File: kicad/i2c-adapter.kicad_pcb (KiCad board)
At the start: 2 copper layers, 98.4 x 65 mm, 49 parts, among them J1 Conn_02x13_Top_Bottom, J10 AUX IN, J11 +5V, J2 I2C-1, J3 I2C-2, J4 I2C-3, J5 I2C-4, J6 SPI-1, J7 SPI-2, J8 SPI-3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

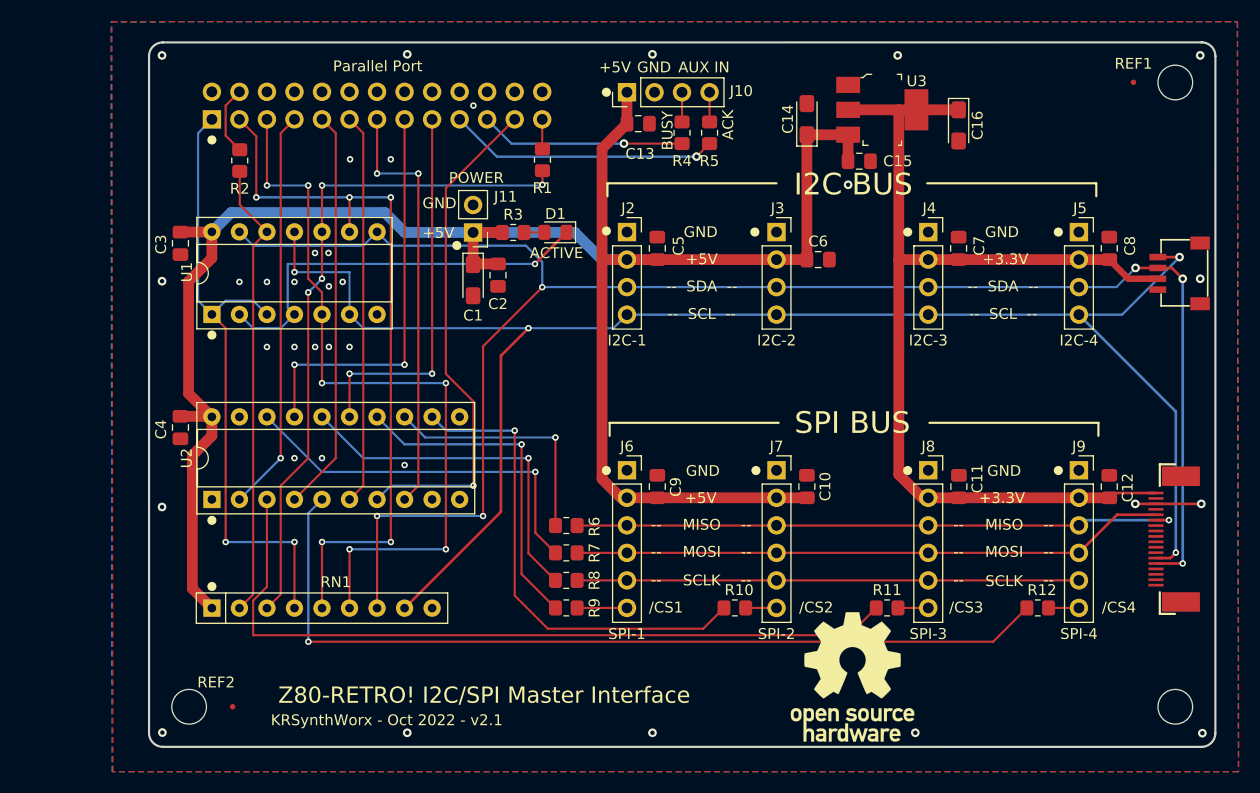
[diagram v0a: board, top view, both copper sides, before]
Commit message: Finish up cleanup of both Schematic and PCB; Give Adafruit connectors labels.
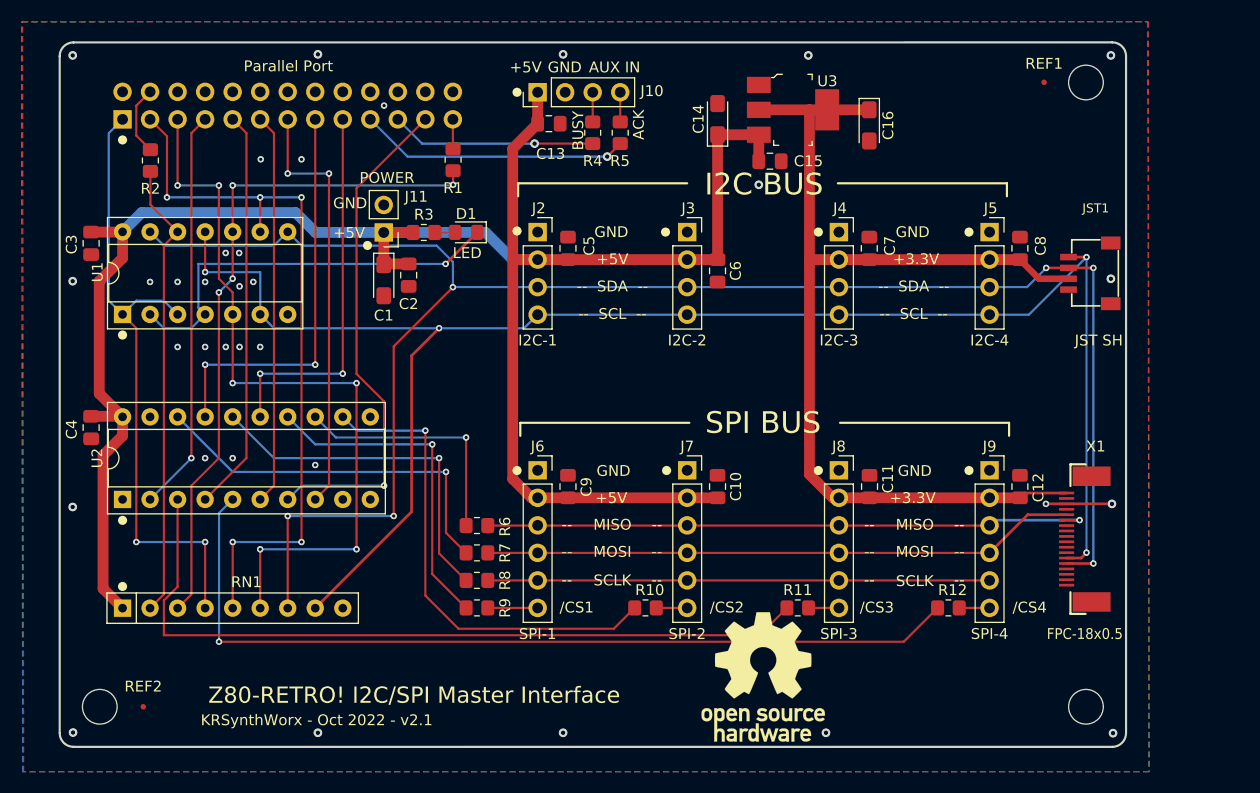
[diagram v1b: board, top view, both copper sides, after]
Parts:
- JST1: renamed from CONN1; value STEMMA_I2C_QT -> JST SH
- X1: value EYE_SPI_DISPLAY_FLIP -> FPC-18x0.5
- moved C6 9.34 mm to (153.5, 86.0), turned to -90 degrees
- moved J5 8.24 mm to (178.6, 82.4)
- moved J9 8.24 mm to (178.6, 104.4)
- moved R1 8.24 mm to (129.1, 75.7)
- moved R10 8.24 mm to (146.8, 117.1)
- moved R4 8.24 mm to (141.9, 73.2)
- moved REF1 8.24 mm to (183.6, 68.6)
- moved C1 8.24 mm to (122.7, 86.8)
- moved C3 8.24 mm to (95.7, 83.4)
- moved C4 8.24 mm to (95.7, 100.4)
- moved J11 8.24 mm to (122.7, 82.4)
- moved R2 8.24 mm to (101.1, 75.8)
- moved REF2 8.24 mm to (100.5, 126.2)
- moved C10 8.24 mm to (153.5, 105.9)
- moved C11 8.24 mm to (167.5, 105.9)
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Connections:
- X1 pad 10: /CARDCS -> unconnected-(X1-Pad10)
- X1 pad 11: /MEM_CS -> unconnected-(X1-Pad11)
- X1 pad 12: /TSCS -> unconnected-(X1-Pad12)
- X1 pad 15: /INT -> unconnected-(X1-Pad15)
- X1 pad 16: /BUSY2 -> unconnected-(X1-Pad16)
- X1 pad 17: /GPIO1 -> unconnected-(X1-Pad17)
- X1 pad 18: /GPIO2 -> unconnected-(X1-Pad18)
- X1 pad 2: /LITE -> unconnected-(X1-Pad2)
- X1 pad 7: /TFTDC -> unconnected-(X1-Pad7)
- X1 pad 8: /TFTRST -> unconnected-(X1-Pad8)
- X1 pad 9: /TFTCS -> unconnected-(X1-Pad9)
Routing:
- net /SCL: track 152.8 -> 153.7 mm
- net /SDA: track 163.1 -> 163.7 mm
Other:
- board text added: "LED"
- board text removed: "ACTIVE"

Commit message: Update PCB Render
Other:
- board text added: "KRSynthWorx - Mar 2023 - v2.1"
- board text removed: "KRSynthWorx - Oct 2022 - v2.1"
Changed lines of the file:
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@@
     (effects (font (size 1 1) (thickness 0.15)))
   )
-  (gr_text "KRSynthWorx - Oct 2022 - v2.1" (at 116.470661 127.4375) (layer "F.SilkS")
+  (gr_text "KRSynthWorx - Mar 2023 - v2.1" (at 116.470661 127.4375) (layer "F.SilkS")
     (effects (font (size 1 1) (thickness 0.15)))
   )

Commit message: Make the Adafruit connectors easier to understand; Label sockets with Chip Part #
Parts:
- renumbered X1 to EyeSPI1, JST1 to StemmaQT1
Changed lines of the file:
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@@
   (net 43 "unconnected-(U2-Pad9)")
   (net 44 "Net-(R12-Pad1)")
-  (net 45 "unconnected-(X1-Pad2)")
+  (net 45 "unconnected-(EyeSPI1-Pad2)")
   (net 46 "/SCK")
-  (net 47 "unconnected-(X1-Pad7)")
-  (net 48 "unconnected-(X1-Pad8)")
-  (net 49 "unconnected-(X1-Pad9)")
-  (net 50 "unconnected-(X1-Pad10)")
-  (net 51 "unconnected-(X1-Pad11)")
-  (net 52 "unconnected-(X1-Pad12)")
-  (net 53 "unconnected-(X1-Pad15)")
-  (net 54 "unconnected-(X1-Pad16)")
-  (net 55 "unconnected-(X1-Pad17)")
-  (net 56 "unconnected-(X1-Pad18)")
+  (net 47 "unconnected-(EyeSPI1-Pad7)")
+  (net 48 "unconnected-(EyeSPI1-Pad8)")
+  (net 49 "unconnected-(EyeSPI1-Pad9)")
+  (net 50 "unconnected-(EyeSPI1-Pad10)")
+  (net 51 "unconnected-(EyeSPI1-Pad11)")
+  (net 52 "unconnected-(EyeSPI1-Pad12)")
+  (net 53 "unconnected-(EyeSPI1-Pad15)")
+  (net 54 "unconnected-(EyeSPI1-Pad16)")
+  (net 55 "unconnected-(EyeSPI1-Pad17)")
+  (net 56 "unconnected-(EyeSPI1-Pad18)")
   (footprint "Connector_PinHeader_2.54mm:PinHeader_1x02_P2.54mm_Vertical" (layer "F.Cu")
     (at 122.656661 82.4375 180)
@@
       (effects (font (size 1 1) (thickness 0.15)))
     )
-    (fp_text value "74HC05" (at 3.81 17.57 90) (layer "F.Fab")
+    (fp_text value "74HC05" (at 3.81 17.57 90) (layer "F.SilkS")
       (effects (font (size 1 1) (thickness 0.15)))
     )
@@
       (effects (font (size 1 1) (thickness 0.15)))
     )
-    (fp_text value "74HC244" (at 3.81 25.19 90) (layer "F.Fab")
+    (fp_text value "74HC244" (at 3.81 25.19 90) (layer "F.SilkS")
       (effects (font (size 1 1) (thickness 0.15)))
     )
@@
       (effects (font (size 1 1) (thickness 0.15)))
     )
-    (fp_text value "0.1uF" (at 3.3845 1.68 180) (layer "F.Fab")
+    (fp_text value "0.1uF" (at 2.1145 3.047339 180) (layer "F.Fab")
       (effects (font (size 1 1) (thickness 0.15)))
     )
@@
     (property "Sheetfile" "i2c-adapter.kicad_sch")
     (property "Sheetname" "")
-    (fp_text reference "X1" (at 8.55 1.536 180) (layer "F.SilkS")
-      (effects (font (size 1 1) (thickness 0.15)))
+    (fp_text reference "EyeSPI1" (at 8.55 4.04 180) (layer "F.SilkS")
+      (effects (font (size 1 1) (thickness 0.15)) (justify right))
     )
-    (fp_text value "FPC-18x0.5" (at -8.75 4.04 180) (layer "F.SilkS")
+    (fp_text value "FPC-18x0.5" (at -10.25 4.04 180) (layer "F.SilkS")
       (effects (font (size 1 0.9) (thickness 0.15)) (justify right))
     )
@@
       (net 36 "+3V3") (pinfunction "VCC") (pintype "power_in") (solder_mask_margin 0.0508))
     (pad "2" smd rect (at 3.75 -1.154 270) (size 0.25 1.4) (layers "F.Cu" "F.Paste" "F.Mask")
-      (net 45 "unconnected-(X1-Pad2)") (pinfunction "BACKLITE") (pintype "input+no_connect") (solder_mask_margin 0.0508))
+      (net 45 "unconnected-(EyeSPI1-Pad2)") (pinfunction "BACKLITE") (pintype "input+no_connect") (solder_mask_margin 0.0508))
     (pad "3" smd rect (at 3.25 -1.154 270) (size 0.25 1.4) (layers "F.Cu" "F.Paste" "F.Mask")
       (net 2 "GND") (pinfunction "GND") (pintype "power_in") (solder_mask_margin 0.0508))
@@
       (net 28 "/MISO") (pinfunction "MISO") (pintype "output") (solder_mask_margin 0.0508))
     (pad "7" smd rect (at 1.25 -1.154 270) (size 0.25 1.4) (layers "F.Cu" "F.Paste" "F.Mask")
-      (net 47 "unconnected-(X1-Pad7)") (pinfunction "DC") (pintype "input+no_connect") (solder_mask_margin 0.0508))
+      (net 47 "unconnected-(EyeSPI1-Pad7)") (pinfunction "DC") (pintype "input+no_connect") (solder_mask_margin 0.0508))
     (pad "8" smd rect (at 0.75 -1.154 270) (size 0.25 1.4) (layers "F.Cu" "F.Paste" "F.Mask")
-      (net 48 "unconnected-(X1-Pad8)") (pinfunction "RESET") (pintype "input+no_connect") (solder_mask_margin 0.0508))
+      (net 48 "unconnected-(EyeSPI1-Pad8)") (pinfunction "RESET") (pintype "input+no_connect") (solder_mask_margin 0.0508))
     (pad "9" smd rect (at 0.25 -1.154 270) (size 0.25 1.4) (layers "F.Cu" "F.Paste" "F.Mask")
-      (net 49 "unconnected-(X1-Pad9)") (pinfunction "DISP_CS") (pintype "input+no_connect") (solder_mask_margin 0.0508))
+      (net 49 "unconnected-(EyeSPI1-Pad9)") (pinfunction "DISP_CS") (pintype "input+no_connect") (solder_mask_margin 0.0508))
     (pad "10" smd rect (at -0.25 -1.154 270) (size 0.25 1.4) (layers "F.Cu" "F.Paste" "F.Mask")
-      (net 50 "unconnected-(X1-Pad10)") (pinfunction "SD_CS") (pintype "input+no_connect") (solder_mask_margin 0.0508))
+      (net 50 "unconnected-(EyeSPI1-Pad10)") (pinfunction "SD_CS") (pintype "input+no_connect") (solder_mask_margin 0.0508))
     (pad "11" smd rect (at -0.75 -1.154 270) (size 0.25 1.4) (layers "F.Cu" "F.Paste" "F.Mask")
-      (net 51 "unconnected-(X1-Pad11)") (pinfunction "MEM_CS") (pintype "input+no_connect") (solder_mask_margin 0.0508))
+      (net 51 "unconnected-(EyeSPI1-Pad11)") (pinfunction "MEM_CS") (pintype "input+no_connect") (solder_mask_margin 0.0508))
     (pad "12" smd rect (at -1.25 -1.154 270) (size 0.25 1.4) (layers "F.Cu" "F.Paste" "F.Mask")
-      (net 52 "unconnected-(X1-Pad12)") (pinfunction "TS_CS") (pintype "input+no_connect") (solder_mask_margin 0.0508))
+      (net 52 "unconnected-(EyeSPI1-Pad12)") (pinfunction "TS_CS") (pintype "input+no_connect") (solder_mask_margin 0.0508))
     (pad "13" smd rect (at -1.75 -1.154 270) (size 0.25 1.4) (layers "F.Cu" "F.Paste" "F.Mask")
       (net 23 "/SCL") (pinfunction "SCL") (pintype "input") (solder_mask_margin 0.0508))
@@
       (net 22 "/SDA") (pinfunction "SDA") (pintype "bidirectional") (solder_mask_margin 0.0508))
     (pad "15" smd rect (at -2.75 -1.154 270) (size 0.25 1.4) (layers "F.Cu" "F.Paste" "F.Mask")
-      (net 53 "unconnected-(X1-Pad15)") (pinfunction "INT") (pintype "output+no_connect") (solder_mask_margin 0.0508))
+      (net 53 "unconnected-(EyeSPI1-Pad15)") (pinfunction "INT") (pintype "output+no_connect") (solder_mask_margin 0.0508))
     (pad "16" smd rect (at -3.25 -1.154 270) (size 0.25 1.4) (layers "F.Cu" "F.Paste" "F.Mask")
-      (net 54 "unconnected-(X1-Pad16)") (pinfunction "BUSY/TE") (pintype "output+no_connect") (solder_mask_margin 0.0508))
+      (net 54 "unconnected-(EyeSPI1-Pad16)") (pinfunction "BUSY/TE") (pintype "output+no_connect") (solder_mask_margin 0.0508))
     (pad "17" smd rect (at -3.75 -1.154 270) (size 0.25 1.4) (layers "F.Cu" "F.Paste" "F.Mask")
-      (net 55 "unconnected-(X1-Pad17)") (pinfunction "GPIO1") (pintype "passive+no_connect") (solder_mask_margin 0.0508))
+      (net 55 "unconnected-(EyeSPI1-Pad17)") (pinfunction "GPIO1") (pintype "passive+no_connect") (solder_mask_margin 0.0508))
     (pad "18" smd rect (at -4.25 -1.154 270) (size 0.25 1.4) (layers "F.Cu" "F.Paste" "F.Mask")
-      (net 56 "unconnected-(X1-Pad18)") (pinfunction "GPIO2") (pintype "passive+no_connect") (solder_mask_margin 0.0508))
+      (net 56 "unconnected-(EyeSPI1-Pad18)") (pinfunction "GPIO2") (pintype "passive+no_connect") (solder_mask_margin 0.0508))
     (pad "SUPPORT1" smd rect (at -5.8 1.152 90) (size 1.8 3.5) (layers "F.Cu" "F.Paste" "F.Mask")
       (net 2 "GND") (pinfunction "GND") (pintype "power_in") (solder_mask_margin 0.0508))
@@
     (property "Sheetfile" "i2c-adapter.kicad_sch")
     (property "Sheetname" "")
-    (fp_text reference "JST1" (at 6.01 0) (layer "F.SilkS")
-      (effects (font (size 0.829056 0.829056) (thickness 0.186944)))
+    (fp_text reference "StemmaQT1" (at 6.01 2.504) (layer "F.SilkS")
+      (effects (font (size 0.829056 0.829056) (thickness 0.186944)) (justify right))
     )
     (fp_text value "JST SH" (at -6.19 2.504 180) (layer "F.SilkS")
